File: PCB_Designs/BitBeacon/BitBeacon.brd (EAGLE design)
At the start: 30.5 x 33 mm, 94 parts, among them IC1 AD8603UJ, IC2 AD8603UJ, IC3 AD8603UJ, IC4 AD8603UJ

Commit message: updates
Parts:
- R1, R17, R25, R9: value 1M -> 1k
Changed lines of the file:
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@@
 <?xml version="1.0" encoding="utf-8"?>
 <!DOCTYPE eagle SYSTEM "eagle.dtd">
-<eagle version="7.3.0">
+<eagle version="7.4.0">
 <drawing>
 <settings>
@@
 <attribute name="VALUE" x="12.0904" y="-1.143" size="1.27" layer="27"/>
 </element>
-<element name="R1" library="resistor" package="R0402" value="1M" x="11.0236" y="4.9276" smashed="yes" rot="R90">
+<element name="R1" library="resistor" package="R0402" value="1k" x="11.0236" y="4.9276" smashed="yes" rot="R90">
 <attribute name="NAME" x="10.3886" y="4.2926" size="1.27" layer="25" rot="R90"/>
 <attribute name="VALUE" x="12.9286" y="4.2926" size="1.27" layer="27" rot="R90"/>
@@
 <attribute name="VALUE" x="18.415" y="31.115" size="1.27" layer="27" rot="R180"/>
 </element>
-<element name="R9" library="resistor" package="R0402" value="1M" x="19.7612" y="24.4348" smashed="yes" rot="R270">
+<element name="R9" library="resistor" package="R0402" value="1k" x="19.7612" y="24.4348" smashed="yes" rot="R270">
 <attribute name="NAME" x="20.3962" y="25.0698" size="1.27" layer="25" rot="R270"/>
 <attribute name="VALUE" x="17.8562" y="25.0698" size="1.27" layer="27" rot="R270"/>
@@
 <attribute name="VALUE" x="-1.016" y="12.065" size="1.27" layer="28" rot="MR90"/>
 </element>
-<element name="R17" library="resistor" package="R0402" value="1M" x="5.8928" y="9.8044" smashed="yes" rot="MR180">
+<element name="R17" library="resistor" package="R0402" value="1k" x="5.8928" y="9.8044" smashed="yes" rot="MR180">
 <attribute name="NAME" x="5.2578" y="9.1694" size="1.27" layer="26" rot="MR180"/>
 <attribute name="VALUE" x="5.2578" y="11.7094" size="1.27" layer="28" rot="MR180"/>
@@
 <attribute name="VALUE" x="30.7848" y="18.5928" size="1.27" layer="28" rot="MR270"/>
 </element>
-<element name="R25" library="resistor" package="R0402" value="1M" x="24.384" y="19.7358" smashed="yes" rot="MR0">
+<element name="R25" library="resistor" package="R0402" value="1k" x="24.384" y="19.7358" smashed="yes" rot="MR0">
 <attribute name="NAME" x="25.019" y="20.3708" size="1.27" layer="26" rot="MR0"/>
 <attribute name="VALUE" x="25.019" y="17.8308" size="1.27" layer="28" rot="MR0"/>

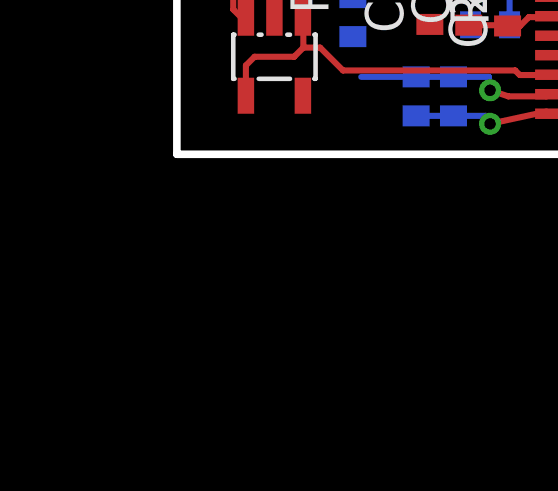
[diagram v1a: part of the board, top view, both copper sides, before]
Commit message: added resistor to peak detector circuit to discharge capacitor
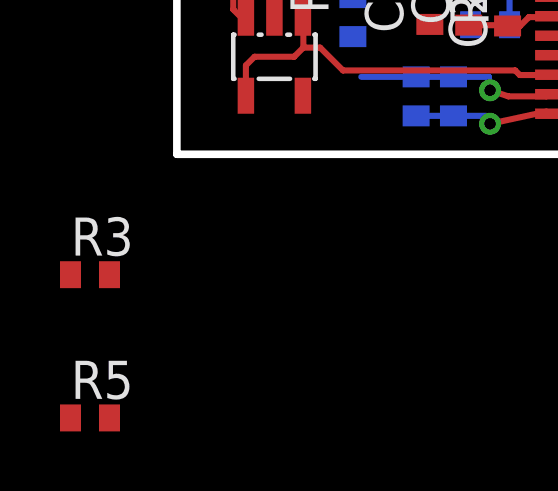
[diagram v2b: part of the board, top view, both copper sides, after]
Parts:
- added R3, R5: 1M, resistor:R0402
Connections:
- net GND: now also R3.1, R5.1
- net N-OUT: now also R3.2
- net S-OUT: now also R5.2
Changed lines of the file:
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@@
 <?xml version="1.0" encoding="utf-8"?>
 <!DOCTYPE eagle SYSTEM "eagle.dtd">
-<eagle version="7.4.0">
+<eagle version="7.3.0">
 <drawing>
 <settings>
@@
 </element>
 <element name="LOGO1" library="SparkFun-Aesthetics" package="OSHW-LOGO-S" value="OSHW-LOGOS" x="2.54" y="30.8356" smashed="yes"/>
+<element name="R3" library="resistor" package="R0402" value="1M" x="-2.8956" y="-4.0132"/>
+<element name="R5" library="resistor" package="R0402" value="1M" x="-2.8956" y="-8.7884"/>
 </elements>
 <signals>
@@
 <wire x1="3.2512" y1="4.5512" x2="3.2512" y2="5.0292" width="0.2032" layer="1"/>
 <wire x1="3.2512" y1="5.0292" x2="4.2164" y2="5.9944" width="0.2032" layer="1"/>
+<contactref element="R3" pad="1"/>
+<contactref element="R5" pad="1"/>
+<wire x1="28.1732" y1="27.686" x2="28.0566" y2="30.0228" width="0" layer="19" extent="16-16"/>
+<wire x1="26.7312" y1="23.9776" x2="28.1732" y2="27.686" width="0" layer="19" extent="16-16"/>
+<wire x1="28.1582" y1="18.4404" x2="26.7312" y2="23.9776" width="0" layer="19" extent="1-16"/>
+<wire x1="22.0472" y1="30.9372" x2="28.0566" y2="30.0228" width="0" layer="19" extent="16-16"/>
+<wire x1="22.0876" y1="18.6944" x2="28.1582" y2="18.4404" width="0" layer="19" extent="1-16"/>
+<wire x1="22.987" y1="14.986" x2="22.0876" y2="18.6944" width="0" layer="19" extent="1-16"/>
+<wire x1="18.6436" y1="14.2448" x2="21.971" y2="13.97" width="0" layer="19" extent="16-16"/>
+<wire x1="16.3576" y1="16.2964" x2="18.6436" y2="14.2448" width="0" layer="19" extent="16-16"/>
+<wire x1="26.3398" y1="12.5428" x2="22.987" y2="14.986" width="0" layer="19" extent="1-16"/>
+<wire x1="21.732" y1="9.4234" x2="21.971" y2="13.97" width="0" layer="19" extent="16-16"/>
+<wire x1="19.7716" y1="7.6454" x2="21.732" y2="9.4234" width="0" layer="19" extent="1-16"/>
+<wire x1="18.1404" y1="3.302" x2="18.4404" y2="7.112" width="0" layer="19" extent="1-1"/>
+<wire x1="13.97" y1="8.509" x2="18.4404" y2="7.112" width="0" layer="19" extent="1-1"/>
+<wire x1="12.2324" y1="12.446" x2="13.97" y2="8.509" width="0" layer="19" extent="16-16"/>
+<wire x1="11.7348" y1="14.3972" x2="12.2324" y2="12.446" width="0" layer="19" extent="16-16"/>
+<wire x1="8.509" y1="16.51" x2="11.7348" y2="14.3972" width="0" layer="19" extent="16-16"/>
+<wire x1="10.0688" y1="18.7452" x2="8.509" y2="16.51" width="0" layer="19" extent="16-16"/>
+<wire x1="8.0264" y1="10.2108" x2="12.2324" y2="12.446" width="0" layer="19" extent="16-16"/>
+<wire x1="3.7442" y1="7.7874" x2="6.4666" y2="11.1252" width="0" layer="19" extent="1-1"/>
+<wire x1="4.2164" y1="5.9944" x2="4.3688" y2="7.1628" width="0" layer="19" extent="1-1"/>
+<wire x1="9.7894" y1="4.318" x2="5.6388" y2="5.8524" width="0" layer="19" extent="1-16"/>
+<wire x1="3.429" y1="18.115" x2="8.509" y2="16.51" width="0" layer="19" extent="16-16"/>
+<wire x1="16.51" y1="21.971" x2="16.3576" y2="16.2964" width="0" layer="19" extent="16-16"/>
+<wire x1="16.7282" y1="24.0284" x2="16.51" y2="21.971" width="0" layer="19" extent="16-16"/>
+<wire x1="12.365" y1="26.67" x2="16.7282" y2="24.0284" width="0" layer="19" extent="1-16"/>
+<wire x1="6.8072" y1="30.9372" x2="10.8712" y2="26.67" width="0" layer="19" extent="1-1"/>
+<wire x1="4.2164" y1="25.7706" x2="6.8072" y2="30.9372" width="0" layer="19" extent="16-16"/>
+<wire x1="4.43" y1="25.3746" x2="4.2164" y2="25.7706" width="0" layer="19" extent="1-16"/>
+<wire x1="-3.5456" y1="-4.0132" x2="3.2512" y2="4.5512" width="0" layer="19" extent="1-1"/>
+<wire x1="-3.5456" y1="-8.7884" x2="-3.5456" y2="-4.0132" width="0" layer="19" extent="1-1"/>
 </signal>
 <signal name="5V">
@@
 <wire x1="19.3548" y1="22.098" x2="18.6944" y2="22.7584" width="0.2032" layer="16"/>
 <wire x1="21.2818" y1="11.6874" x2="20.32" y2="12.6492" width="0.2032" layer="1"/>
+<contactref element="R3" pad="2"/>
+<wire x1="-2.2456" y1="-4.0132" x2="21.0716" y2="7.6454" width="0" layer="19" extent="1-1"/>
 </signal>
 <signal name="N$4">
@@
 <wire x1="7.0104" y1="26.1112" x2="7.0104" y2="26.5684" width="0.2032" layer="16"/>
 <wire x1="7.0104" y1="26.5684" x2="8.4836" y2="28.0416" width="0.2032" layer="16"/>
+<contactref element="R5" pad="2"/>
+<wire x1="-2.2456" y1="-8.7884" x2="5.9874" y2="23.8506" width="0" layer="19" extent="1-1"/>
 </signal>
 <signal name="N$19">

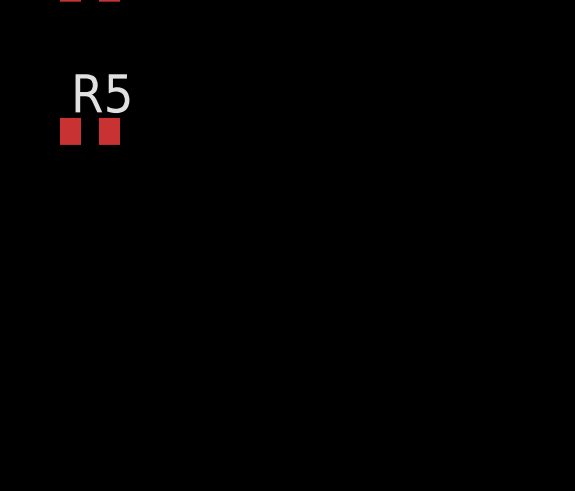
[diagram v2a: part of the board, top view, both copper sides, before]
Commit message: corrections to PCB for BitBeacon, updates on BitController
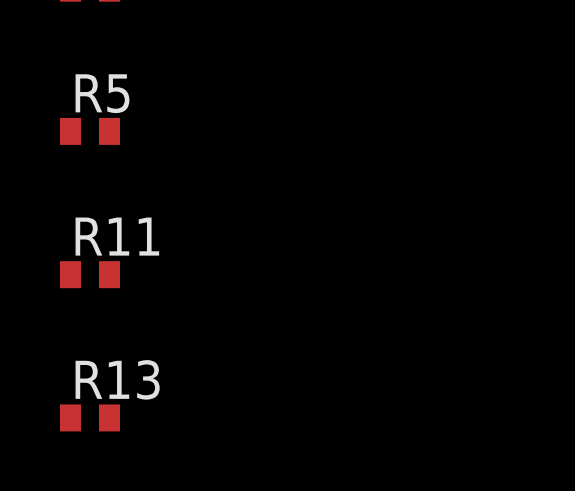
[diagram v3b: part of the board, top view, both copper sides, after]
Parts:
- added R11, R13: 1M, resistor:R0402
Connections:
- net E-OUT: now also R11.2
- net GND: now also R11.1, R13.1
- net W-OUT: now also R13.2
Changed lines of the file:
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@@
 <?xml version="1.0" encoding="utf-8"?>
 <!DOCTYPE eagle SYSTEM "eagle.dtd">
-<eagle version="7.3.0">
+<eagle version="7.4.0">
 <drawing>
 <settings>
@@
 <element name="R3" library="resistor" package="R0402" value="1M" x="-2.8956" y="-4.0132"/>
 <element name="R5" library="resistor" package="R0402" value="1M" x="-2.8956" y="-8.7884"/>
+<element name="R11" library="resistor" package="R0402" value="1M" x="-2.8956" y="-13.5636"/>
+<element name="R13" library="resistor" package="R0402" value="1M" x="-2.8956" y="-18.3388"/>
 </elements>
 <signals>
@@
 <contactref element="R3" pad="1"/>
 <contactref element="R5" pad="1"/>
+<contactref element="R11" pad="1"/>
+<contactref element="R13" pad="1"/>
 <wire x1="28.1732" y1="27.686" x2="28.0566" y2="30.0228" width="0" layer="19" extent="16-16"/>
 <wire x1="26.7312" y1="23.9776" x2="28.1732" y2="27.686" width="0" layer="19" extent="16-16"/>
@@
 <wire x1="-3.5456" y1="-4.0132" x2="3.2512" y2="4.5512" width="0" layer="19" extent="1-1"/>
 <wire x1="-3.5456" y1="-8.7884" x2="-3.5456" y2="-4.0132" width="0" layer="19" extent="1-1"/>
+<wire x1="-3.5456" y1="-13.5636" x2="-3.5456" y2="-8.7884" width="0" layer="19" extent="1-1"/>
+<wire x1="-3.5456" y1="-18.3388" x2="-3.5456" y2="-13.5636" width="0" layer="19" extent="1-1"/>
 </signal>
 <signal name="5V">
@@
 <wire x1="5.1308" y1="27.5336" x2="5.1308" y2="24.4706" width="0.2032" layer="16"/>
 <wire x1="5.1308" y1="24.4706" x2="5.102" y2="24.4418" width="0.2032" layer="16"/>
+<contactref element="R11" pad="2"/>
+<wire x1="-2.2456" y1="-13.5636" x2="4.2164" y2="24.4706" width="0" layer="19" extent="1-16"/>
 </signal>
 <signal name="N$28">
@@
 <via x="18.1356" y="19.6088" extent="1-16" drill="0.381" shape="octagon"/>
 <wire x1="18.1356" y1="19.6088" x2="18.1356" y2="29.7688" width="0.2032" layer="16"/>
+<contactref element="R13" pad="2"/>
+<wire x1="-2.2456" y1="-18.3388" x2="20.432" y2="9.4234" width="0" layer="19" extent="1-16"/>
 </signal>
 <signal name="N$9">
